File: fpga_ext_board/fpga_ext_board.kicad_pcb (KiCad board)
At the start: 2 copper layers, 100 x 100 mm, 8 parts, among them J1 Conn_02x25_Odd_Even, J2 Conn_02x25_Odd_Even, J3 Conn_02x25_Odd_Even, J4 Conn_02x25_Odd_Even

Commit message: continue work
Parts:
- added J5: Conn_02x17_Odd_Even, Connector_PinHeader_2.54mm:PinHeader_2x17_P2.54mm_Vertical, F.Cu at (60.5, 79.5)
- added J6: Conn_01x08_Pin, Connector_PinHeader_2.54mm:PinHeader_1x08_P2.54mm_Vertical, F.Cu at (116.1, 145.6)
- added J7: Conn_01x12_Pin, Connector_PinHeader_2.54mm:PinHeader_1x12_P2.54mm_Vertical, F.Cu at (151.3, 95.8)
- moved J1 11.4 mm to (80.6, 131.6)
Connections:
- J1 pad 10: /E17 -> /R7
- J1 pad 11: /C17 -> /R6
- J1 pad 12: /C18 -> /T5
- J1 pad 13: /G15 -> /R5
- J1 pad 14: /H16 -> /T4
- J1 pad 15: /F15 -> /U6
- J1 pad 16: /G16 -> /U5
- J1 pad 17: /E16 -> /V4
- J1 pad 18: /E15 -> /U4
- J1 pad 19: /D16 -> /V3
- J1 pad 20: /D15 -> /V2
- J1 pad 21: /A17 -> /U2
- J1 pad 22: /B17 -> /U1
- J1 pad 23: /C16 -> /P4
- J1 pad 24: /B16 -> /T3
- J1 pad 25: /A15 -> /R3
- J1 pad 26: /B15 -> /T2
- J1 pad 27: /A14 -> /N4
- J1 pad 28: /B14 -> /P3
- J1 pad 29: /C14 -> /M6
- J1 pad 30: /D14 -> /M5
- J1 pad 31: /C13 -> /L5
- J1 pad 32: /D13 -> /L4
- J1 pad 33: /A13 -> /K3
- J1 pad 34: /C12 -> /K5
- J1 pad 35: /F14 -> /P1
- J1 pad 36: /E13 -> /R1
- J1 pad 37: /B12 -> /N1
- J1 pad 38: /A12 -> /N2
- J1 pad 39: /C11 -> /M2
- J1 pad 40: /B11 -> /M1
- J1 pad 41: /D11 -> /J5
- J1 pad 42: /D10 -> /J4
- J1 pad 43: /C9 -> /J6
- J1 pad 44: /D9 -> /K6
- J1 pad 45: /A10 -> /L2
- J1 pad 46: /B10 -> /L3
- J1 pad 47: /A9 -> /K2
- J1 pad 48: /B9 -> /K1
- J1 pad 5: /F18 -> /V8
- J1 pad 6: /G17 -> /V7
- J1 pad 7: /E18 -> /U7
- J1 pad 8: /F17 -> /V6
- J1 pad 9: /D18 -> /T7
- J2 pad 10: /E17 -> /R7
- J2 pad 11: /C17 -> /R6
- J2 pad 12: /C18 -> /T5
- J2 pad 13: /G15 -> /R5
- J2 pad 14: /H16 -> /T4
- J2 pad 15: /F15 -> /U6
- J2 pad 16: /G16 -> /U5
- J2 pad 17: /E16 -> /V4
- J2 pad 18: /E15 -> /U4
- J2 pad 19: /D16 -> /V3
- J2 pad 20: /D15 -> /V2
- J2 pad 21: /A17 -> /U2
- J2 pad 22: /B17 -> /U1
- J2 pad 23: /C16 -> /P4
- J2 pad 24: /B16 -> /T3
- J2 pad 25: /A15 -> /R3
- J2 pad 26: /B15 -> /T2
- J2 pad 27: /A14 -> /N4
- J2 pad 28: /B14 -> /P3
- J2 pad 29: /C14 -> /M6
- J2 pad 30: /D14 -> /M5
- J2 pad 31: /C13 -> /L5
- J2 pad 32: /D13 -> /L4
- J2 pad 33: /A13 -> /K3
- J2 pad 34: /C12 -> /K5
- J2 pad 35: /F14 -> /P1
- J2 pad 36: /E13 -> /R1
- J2 pad 37: /B12 -> /N1
- J2 pad 38: /A12 -> /N2
- J2 pad 39: /C11 -> /M2
- J2 pad 40: /B11 -> /M1
- J2 pad 41: /D11 -> /J5
- J2 pad 42: /D10 -> /J4
- J2 pad 43: /C9 -> /J6
- J2 pad 44: /D9 -> /K6
- J2 pad 45: /A10 -> /L2
- J2 pad 46: /B10 -> /L3
- J2 pad 47: /A9 -> /K2
- J2 pad 48: /B9 -> /K1
- J2 pad 5: /F18 -> /V8
- J2 pad 6: /G17 -> /V7
- J2 pad 7: /E18 -> /U7
- J2 pad 8: /F17 -> /V6
- J2 pad 9: /D18 -> /T7

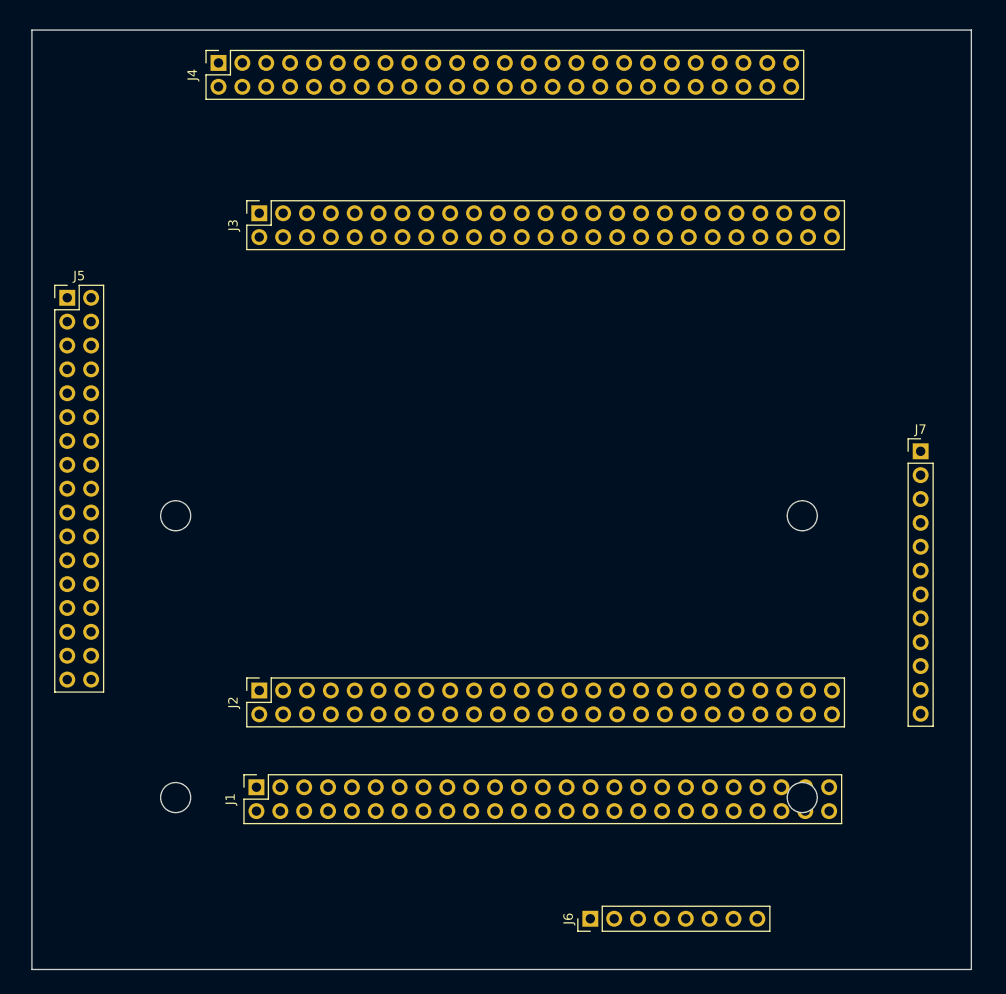
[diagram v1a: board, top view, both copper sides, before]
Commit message: update base board holes
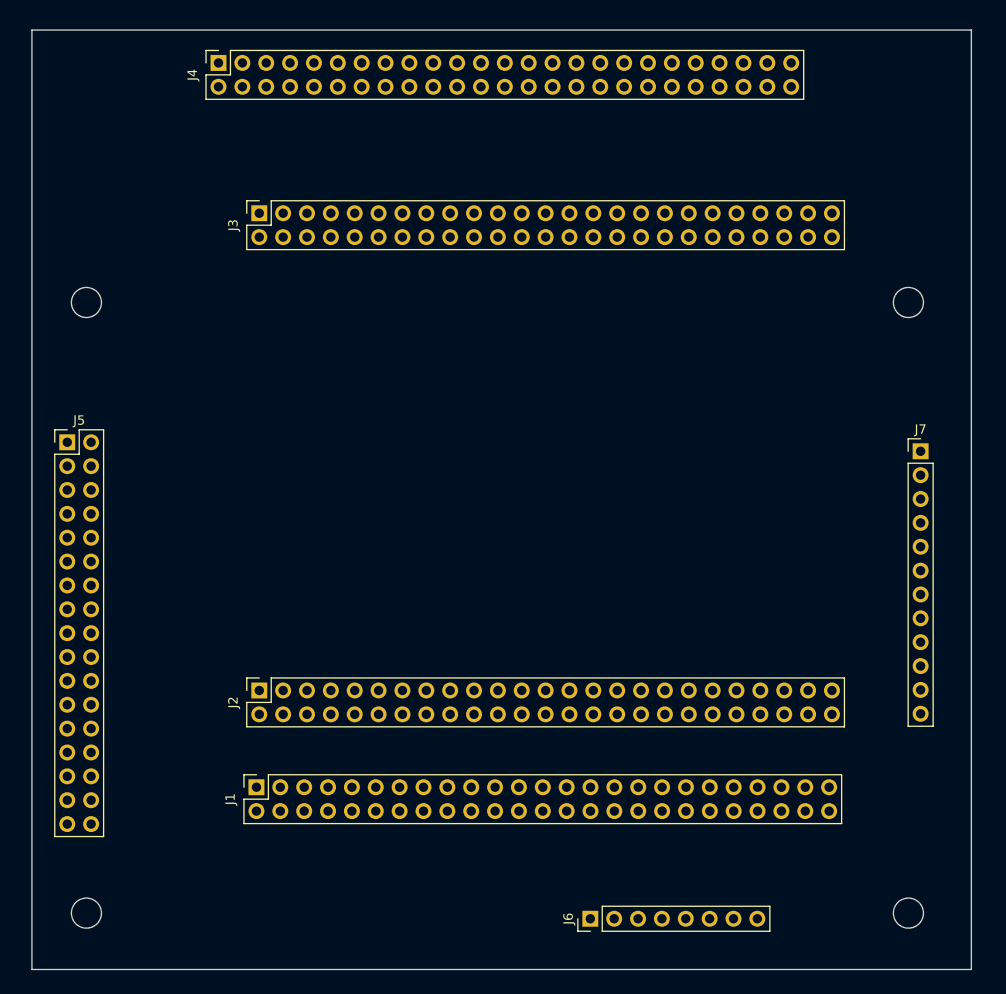
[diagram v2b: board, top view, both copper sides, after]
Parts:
- moved REF2 25.4 mm to (150.0, 80.0)
- moved REF1 24.6 mm to (62.5, 80.0)
- moved REF4 16.7 mm to (150.0, 145.0)
- moved REF3 15.5 mm to (62.5, 145.0)
- moved J5 15.4 mm to (60.5, 94.9)
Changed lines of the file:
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@@
 	(footprint "MountingHole:MountingHole_3.2mm_M3"
 		(layer "F.Cu")
-		(at 138.7 132.7)
+		(at 150 145)
 		(descr "Mounting Hole 3.2mm, no annular, M3")
 		(tags "mounting hole 3.2mm no annular m3")
@@
 		)
 		(fp_text user "${REFERENCE}"
-			(at 0 8.89 360)
+			(at 0 8.89 0)
 			(layer "F.Fab")
 			(effects
@@
 	(footprint "MountingHole:MountingHole_3.2mm_M3"
 		(layer "F.Cu")
-		(at 138.7 102.7)
+		(at 150 80)
 		(descr "Mounting Hole 3.2mm, no annular, M3")
 		(tags "mounting hole 3.2mm no annular m3")
@@
 	(footprint "Connector_PinHeader_2.54mm:PinHeader_2x17_P2.54mm_Vertical"
 		(layer "F.Cu")
-		(at 60.46 79.5)
+		(at 60.46 94.88)
 		(descr "Through hole straight pin header, 2x17, 2.54mm pitch, double rows")
 		(tags "Through hole pin header THT 2x17 2.54mm double row")
@@
 	(footprint "MountingHole:MountingHole_3.2mm_M3"
 		(layer "F.Cu")
-		(at 72 102.7)
+		(at 62.5 80)
 		(descr "Mounting Hole 3.2mm, no annular, M3")
 		(tags "mounting hole 3.2mm no annular m3")
@@
 	(footprint "MountingHole:MountingHole_3.2mm_M3"
 		(layer "F.Cu")
-		(at 72 132.7)
+		(at 62.5 145)
 		(descr "Mounting Hole 3.2mm, no annular, M3")
 		(tags "mounting hole 3.2mm no annular m3")

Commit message: update
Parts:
- added J8: Input, Connector_Molex:Molex_Micro-Fit_3.0_43650-0215_1x02_P3.00mm_Vertical, F.Cu at (151.4, 131.2)
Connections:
- J2 pad 1: +5V -> unconnected-(J2-Pin_1-Pad1)
- J5 pad 22: /T4 -> /T5
- J5 pad 24: /T5 -> /T4
- J5 pad 30: /R7 -> /V6
- J5 pad 32: /V6 -> /R7
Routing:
- net +5V: track 0.00 -> 273.2 mm, vias 0 -> 8
- net /K5: track 0.00 -> 85.1 mm
- net /L4: track 0.00 -> 81.5 mm
- net /M5: track 0.00 -> 77.9 mm
- net /N4: track 0.00 -> 76.5 mm
- net /P3: track 0.00 -> 74.4 mm
- net /R3: track 0.00 -> 72.9 mm
- net /T2: track 0.00 -> 70.7 mm
- net /P4: track 0.00 -> 69.3 mm
- net /T3: track 0.00 -> 67.1 mm
- net /U2: track 0.00 -> 65.7 mm
- net /U1: track 0.00 -> 63.6 mm
- net /V3: track 0.00 -> 62.1 mm
- net /V2: track 0.00 -> 60.2 mm
- net /V4: track 0.00 -> 58.6 mm
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- added copper zone on B.Cu, net +3.3V
- added copper zone on F.Cu, net GND
